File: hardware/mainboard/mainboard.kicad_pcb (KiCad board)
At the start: 4 copper layers, 101 x 38.8 mm, 49 parts, among them J1 2309407-1, J2 WP7B-S040VA1-R6000, J3 Conn_01x02_Male, J4 3-84953-0, J5 503182-1852, J6 WP7B-S040VA1-R6000, U1 TPS65132, U2 MIC5504-1.2YM5-TR, U3 MCP1725-ADJE_MC, U4 TPS65132, U5 ICM-20602

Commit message: start on v0.2
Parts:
- J4: footprint mainboard:TE_3-84953-0 -> mainboard:68713014522
- moved R3 29.6 mm to (169.7, 91.2)
- moved R4 29.6 mm to (170.7, 91.2)
- moved C20 19.6 mm to (179.4, 62.6)
- moved U4 17.8 mm to (174.7, 59.4)
- moved C21 17.2 mm to (177.5, 63.9)
- moved C11 14.4 mm to (110.8, 61.9)
- moved C13 14.4 mm to (112.7, 57.0)
- moved R2 14.4 mm to (115.4, 57.2)
- moved C9 14.4 mm to (116.0, 58.3)
- moved C24 13.1 mm to (162.2, 60.1)
- moved C25 13.1 mm to (162.2, 62.3)
- moved TP1 13.1 mm to (156.3, 61.0)
- moved C23 13.1 mm to (158.2, 59.0)
- moved C26 13.1 mm to (162.2, 61.2)
- moved U5 13.1 mm to (159.2, 61.4)
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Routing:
- net GND: track 336.8 -> 254.4 mm, vias 48 -> 34
- net /SDMMC0_D3: track 55.0 -> 0.00 mm, vias 2 -> 0
- net /SDMMC0_CMD: track 54.9 -> 0.00 mm, vias 2 -> 0
- net /SDMMC0_D2: track 54.2 -> 0.00 mm, vias 2 -> 0
- net /SDMMC0_CLK: track 50.9 -> 0.00 mm
- net /SDMMC0_D1: track 50.8 -> 0.00 mm
- net /SDMMC0_D0: track 49.9 -> 0.00 mm
- net Net-(J5-PadDT): track 35.6 -> 2.91 mm
- net +1V8: track 107.4 -> 86.9 mm, vias 5 -> 2
- net +2V8: track 91.6 -> 74.8 mm, vias 5 -> 2
- net /I2C2_SCL: track 16.4 -> 0.00 mm, vias 2 -> 0
- net /MIPI_CSI1_RST: track 16.2 -> 0.00 mm, vias 2 -> 0
- net /I2C2_SDA: track 16.0 -> 0.00 mm, vias 2 -> 0
- net +3V3: track 35.1 -> 19.4 mm, vias 9 -> 4
- net /MIPI_RX0_D3-: track 15.4 -> 0.07 mm, vias 2 -> 0
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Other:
- board size 101 x 38.8 mm -> 95.8 x 30 mm
- board text added: "JLCJLCJLCJLC"
- board text added: "MR Headset v0.2 © Krishna Mani 2020"
- board text removed: "JLCJLCJLC"
- board text removed: "© Krishna Mani 2020 MR Headset v0.1"

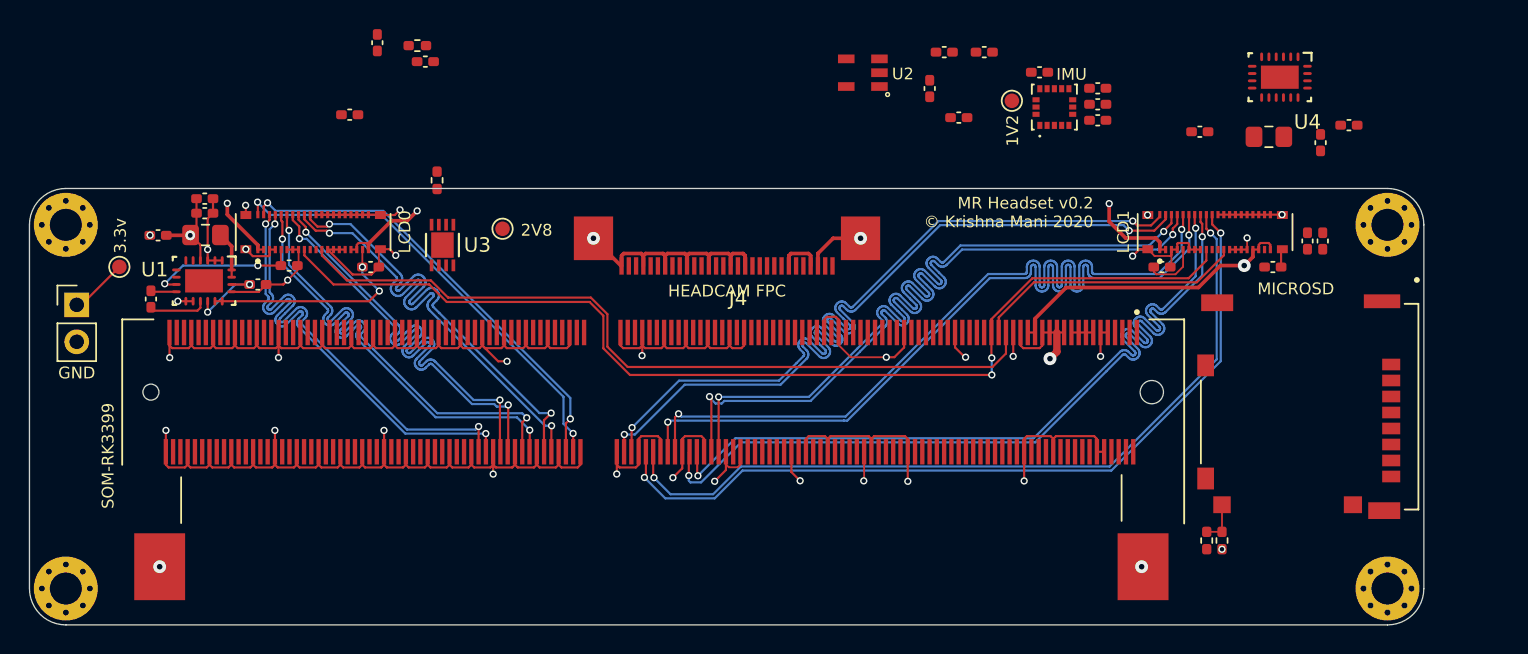
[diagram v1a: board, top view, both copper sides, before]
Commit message: only camera mipi left for v0.2
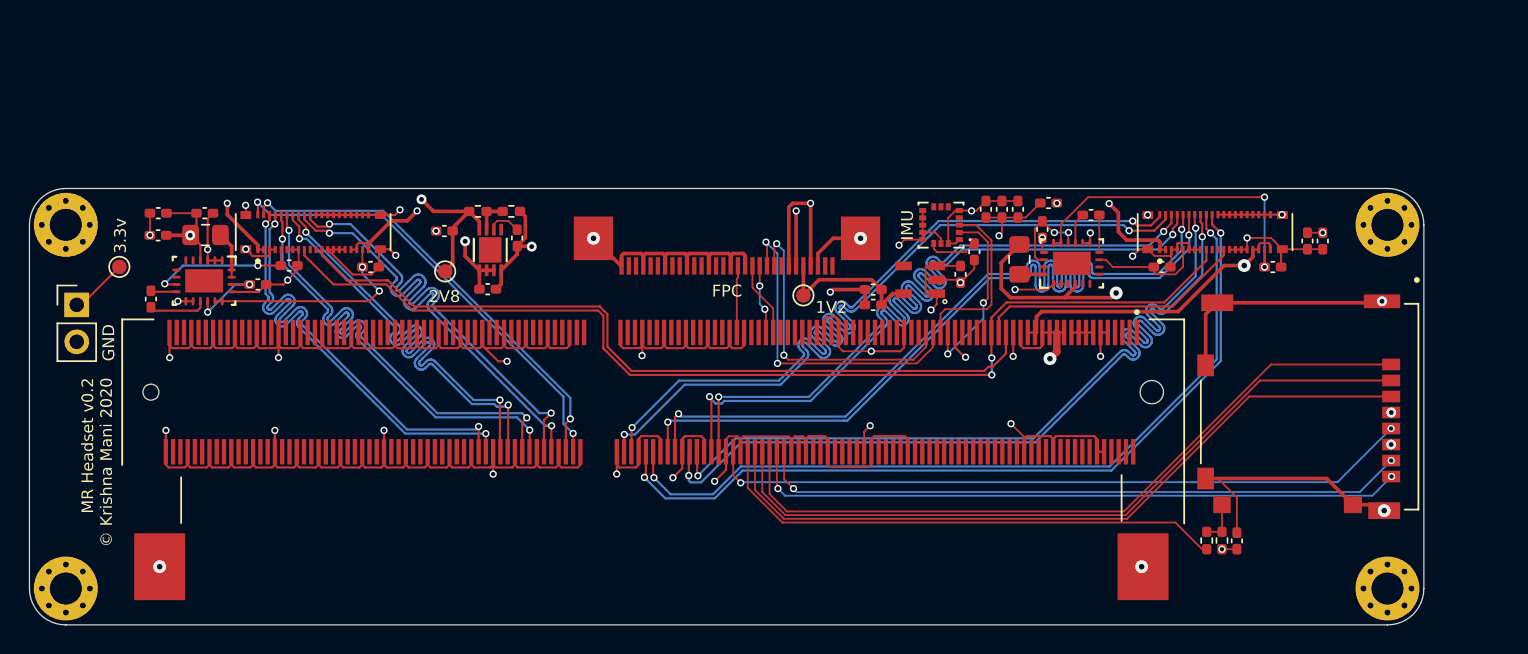
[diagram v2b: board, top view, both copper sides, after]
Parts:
- moved C18 28.2 mm to (171.8, 91.2), turned to 90 degrees
- moved C21 20.0 mm to (158.4, 69.8)
- moved TP1 19.6 mm to (141.9, 74.3)
- moved U4 19.2 mm to (160.4, 72.2), turned to 90 degrees
- moved L2 19.1 mm to (156.8, 71.9), turned to 270 degrees
- moved C20 18.8 mm to (161.7, 68.8), turned to 0 degrees
- moved C10 15.4 mm to (146.8, 75.0), turned to 180 degrees
- moved C6 15.4 mm to (152.8, 72.9), turned to 270 degrees
- moved C11 15.3 mm to (120.2, 73.9), turned to 0 degrees
- moved U2 14.8 mm to (150.0, 73.3)
- moved C13 13.7 mm to (117.3, 69.9), turned to 180 degrees
- moved C9 13.7 mm to (122.3, 70.4), turned to 270 degrees
- moved C7 13.2 mm to (146.8, 74.0), turned to 180 degrees
- moved C23 13.1 mm to (153.7, 71.3), turned to 90 degrees
- moved R2 13.1 mm to (121.9, 68.6)
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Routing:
- net GND: track 254.4 -> 331.3 mm, vias 34 -> 44
- net /SDMMC0_CMD: track 0.00 -> 50.7 mm
- net /SDMMC0_D3: track 0.00 -> 50.5 mm
- net /SDMMC0_D2: track 0.00 -> 50.3 mm
- net /SDMMC0_CLK: track 0.00 -> 48.6 mm, vias 0 -> 2
- net /SDMMC0_D1: track 0.00 -> 45.5 mm, vias 0 -> 2
- net /SDMMC0_D0: track 0.00 -> 44.9 mm, vias 0 -> 2
- net /SDMMC0_DET_L: track 0.00 -> 35.8 mm
- net +3V3: track 19.4 -> 46.5 mm, vias 4 -> 9
- net /LCD 2/AVDD: track 0.00 -> 22.6 mm, vias 0 -> 2
- net /I2C2_SDA: track 0.00 -> 22.5 mm, vias 0 -> 2
- net /I2C2_SCL: track 0.00 -> 20.7 mm, vias 0 -> 2
- net +2V8: track 74.8 -> 91.5 mm, vias 2 -> 5
- net /I2C1_SCL: track 0.00 -> 12.5 mm, vias 0 -> 2
- net /I2C1_SDA: track 0.00 -> 12.1 mm
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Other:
- board text added: "FPC"
- board text removed: "HEADCAM FPC"
- board text removed: "LCD0"
- board text removed: "LCD1"
- board text removed: "MICROSD"
- board text removed: "SOM-RK3399"
